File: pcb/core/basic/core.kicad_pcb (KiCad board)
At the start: 2 copper layers, 79.3 x 78.9 mm, 31 parts, among them J1 Conn_01x11, J2 Conn_01x11, J3 Conn_01x04, SW1 SW_Push_45deg, SW10 RotaryEncoder_Switch, SW11 RotaryEncoder_Switch, SW12 RotaryEncoder_Switch, SW13 RotaryEncoder_Switch, SW2 SW_Push_45deg, SW3 SW_Push_45deg, SW4 SW_Push_45deg, SW5 SW_Push_45deg, SW6 SW_Push_45deg, SW7 SW_Push_45deg, SW8 SW_Push_45deg, SW9 SW_Push_45deg, U1 Helios

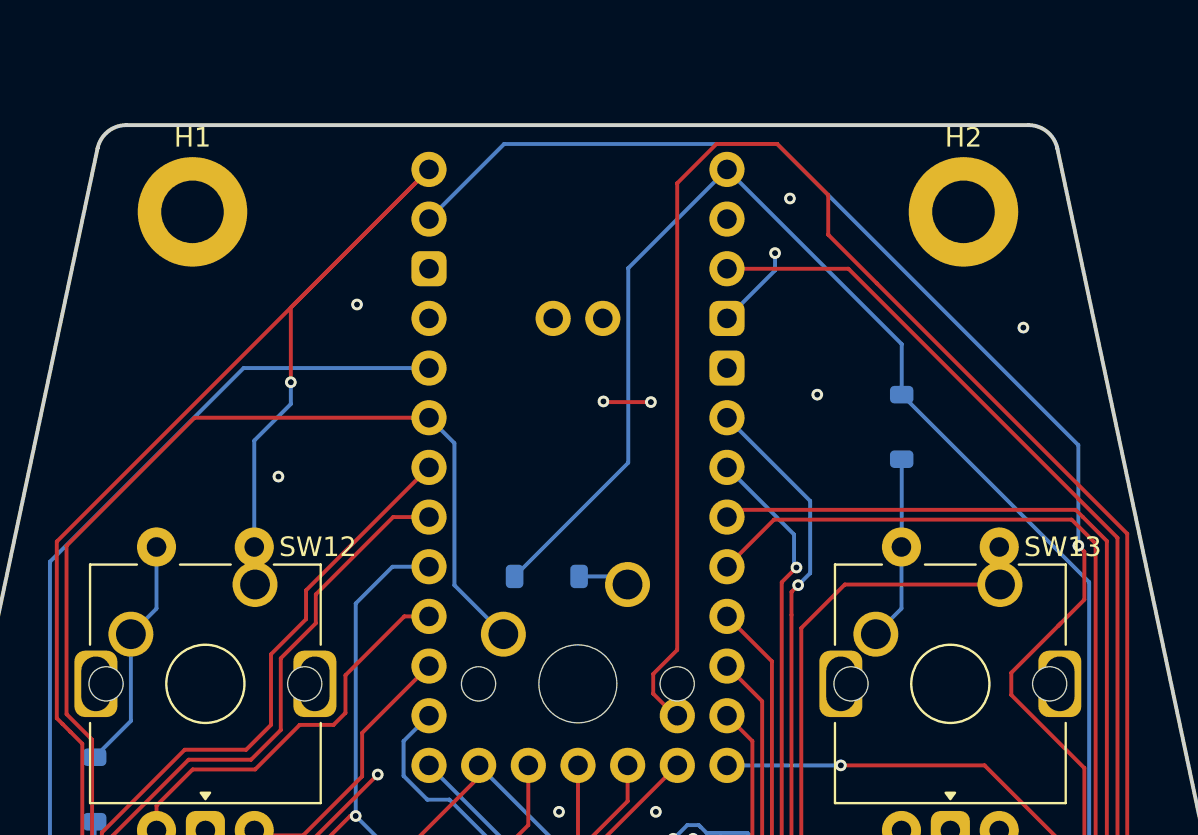
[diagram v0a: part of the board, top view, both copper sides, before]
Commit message: switched rgb back to a regular pin and 3v
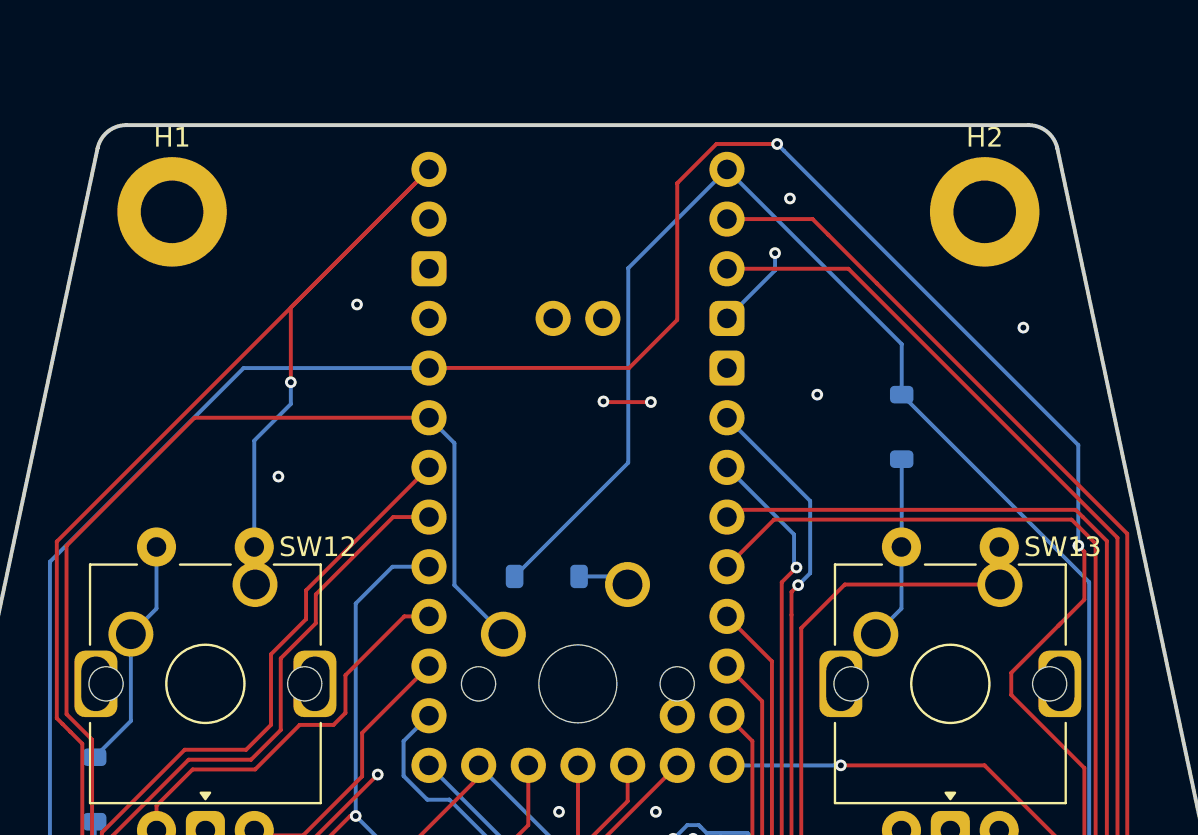
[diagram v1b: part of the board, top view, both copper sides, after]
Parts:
- moved H2 1.09 mm to (219.0, 138.9)
- moved H1 1.04 mm to (177.4, 138.9)
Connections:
- J2 pad 9: raw -> vcc
- U1 pad 1: unconnected-(U1-P0-Pad1) -> rgb
- U1 pad 13: raw -> unconnected-(U1-5V-Pad13)
- U1 pad 34: rgb -> unconnected-(U1-P25-Pad34)
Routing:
- net vcc: track 97.4 -> 203.7 mm, vias 1 -> 3
- net raw: track 99.0 -> 0.00 mm, vias 1 -> 0
- net rgb: track 89.0 -> 54.5 mm

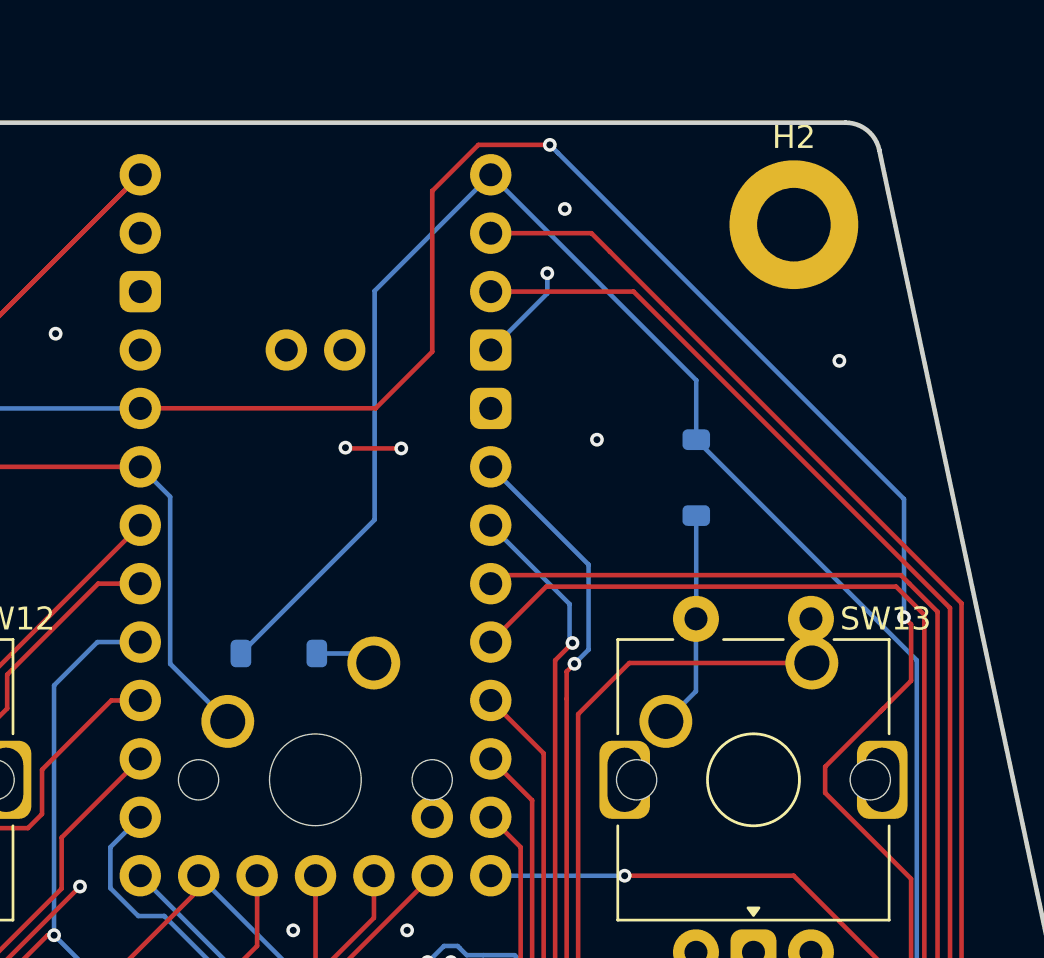
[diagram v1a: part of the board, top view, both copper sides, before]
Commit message: added jumpers for 3.3/5v rgb
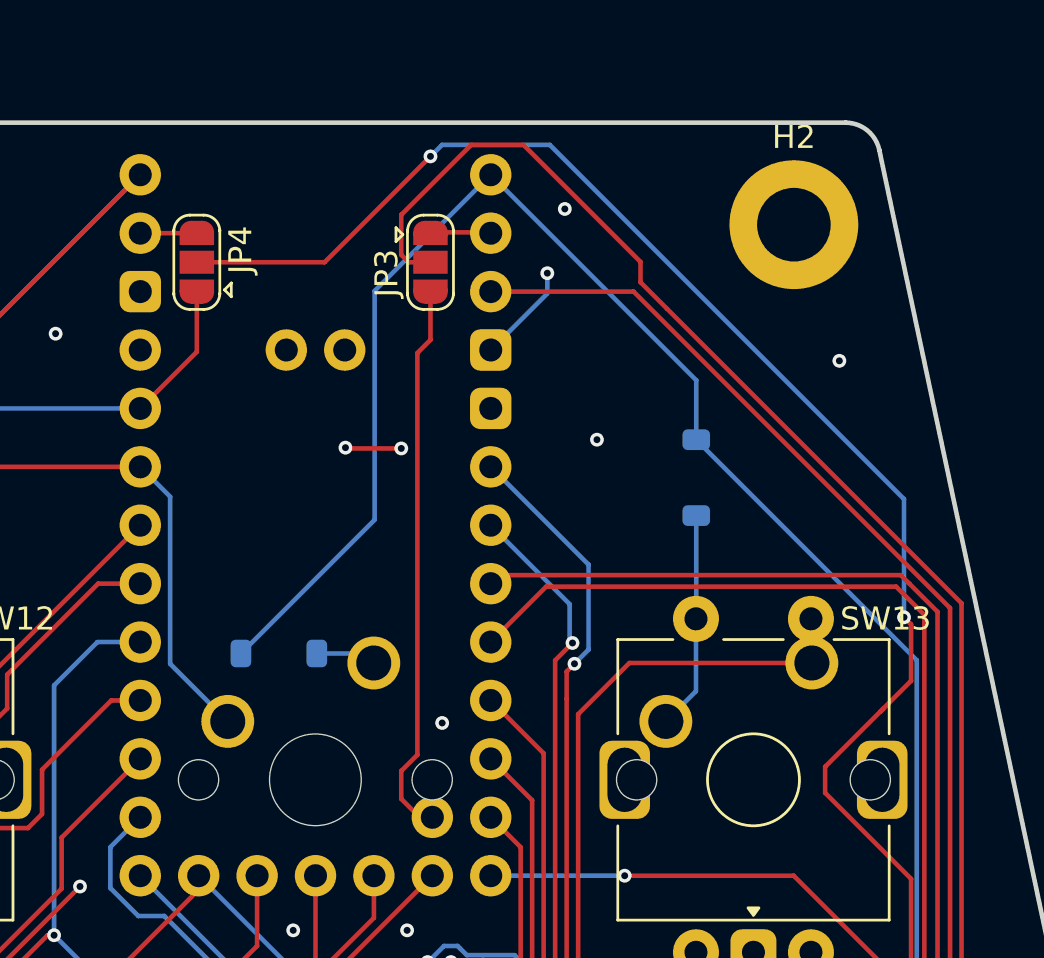
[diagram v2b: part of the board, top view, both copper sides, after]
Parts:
- added JP3: Jumper_3_Open, Jumper:SolderJumper-3_P1.3mm_Open_RoundedPad1.0x1.5mm, F.Cu at (203.2, 140.5)
- added JP4: Jumper_3_Open, Jumper:SolderJumper-3_P1.3mm_Open_RoundedPad1.0x1.5mm, F.Cu at (193.0, 140.5)
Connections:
- J2 pad 9: vcc -> vccrgb
- U1 pad 1: rgb -> Net-(JP3-A)
- U1 pad 13: unconnected-(U1-5V-Pad13) -> Net-(JP4-B)
- U1 pad 34: unconnected-(U1-P25-Pad34) -> Net-(JP3-B)
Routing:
- net vcc: track 203.7 -> 103.5 mm, vias 3 -> 1
- net vccrgb: track 0.00 -> 97.1 mm, vias 0 -> 2
- net Net-(JP3-B): track 0.00 -> 24.3 mm
- net rgb: track 54.5 -> 64.9 mm
- net Net-(JP3-A): track 0.00 -> 2.64 mm
- net Net-(JP4-B): track 0.00 -> 2.53 mm
- net GND: vias 29 -> 30

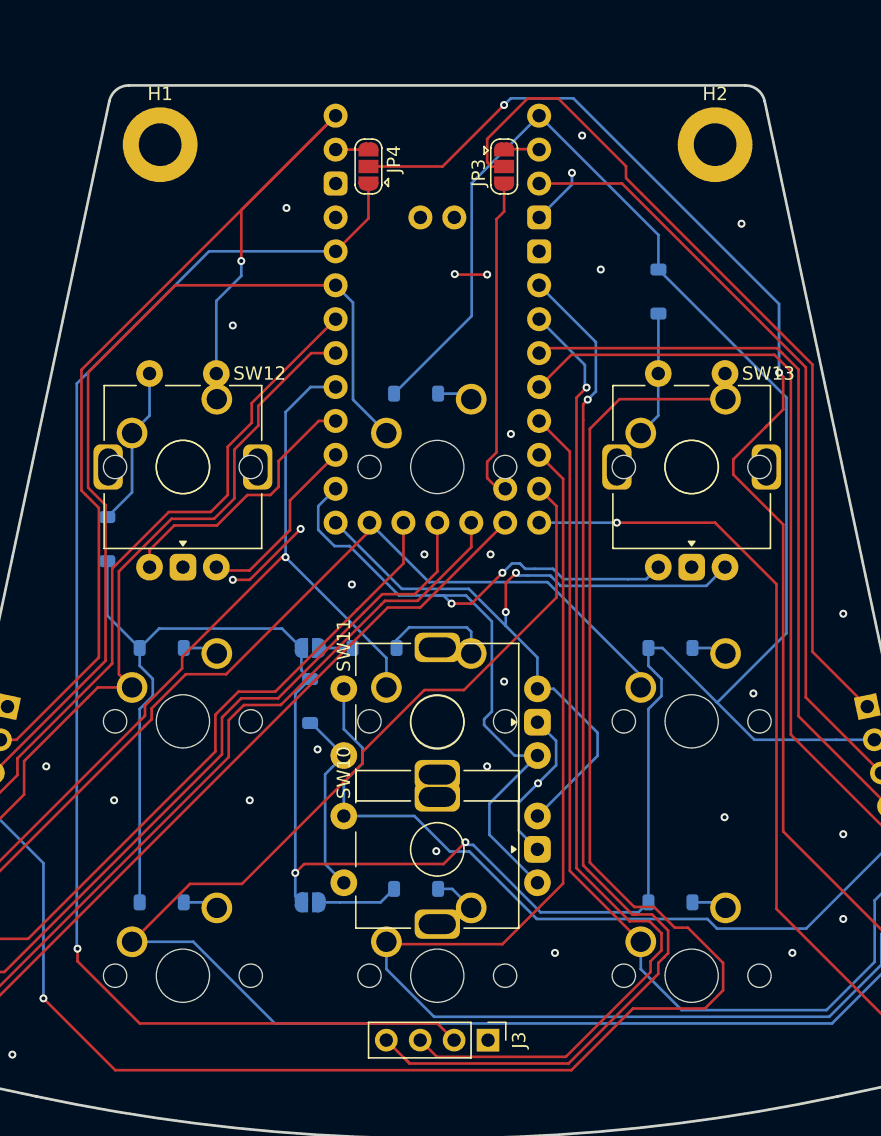
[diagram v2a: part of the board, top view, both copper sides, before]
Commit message: moved rgb jumpers to the other side
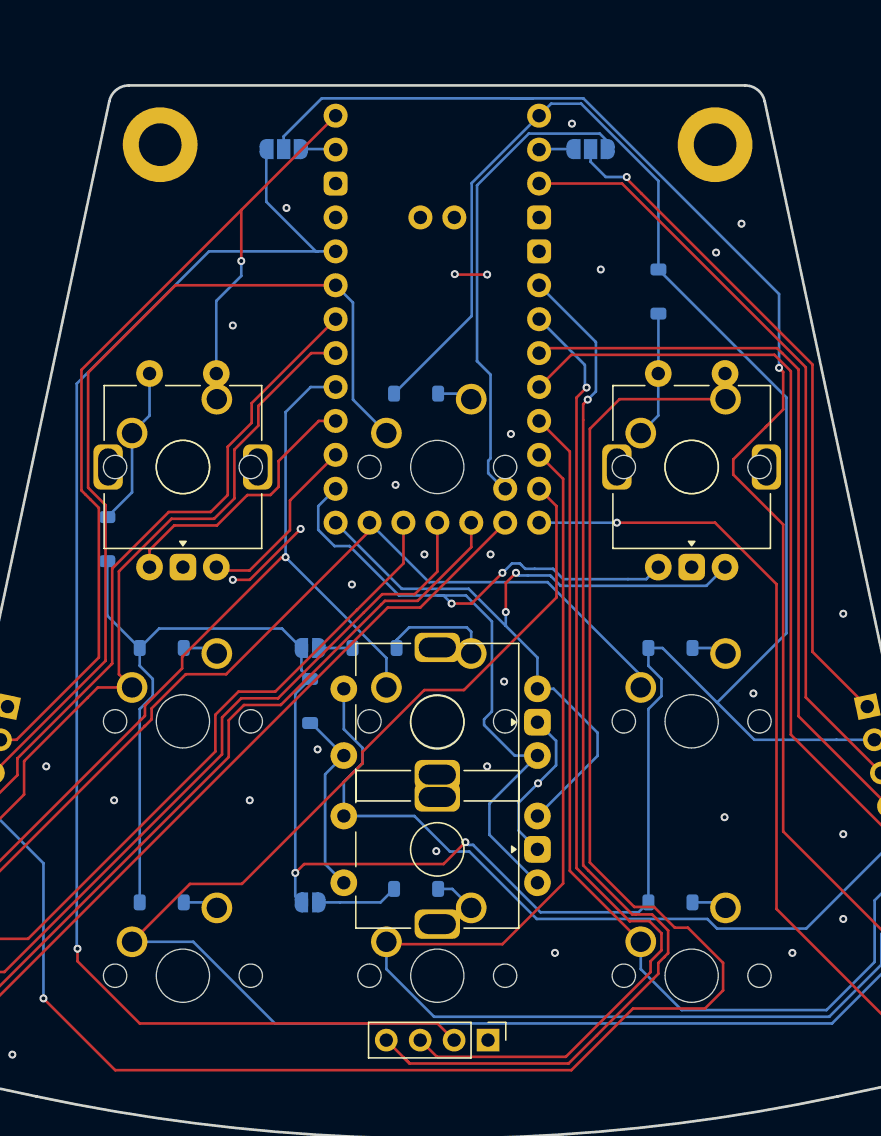
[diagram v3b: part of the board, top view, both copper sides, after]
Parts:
- D1, D10, D2, D3, D4, D5, D6, D7, D8, D9: footprint Diode_SMD:D_SOD-123 -> barnacle:D_SOD-123-minimal
- JP3, JP4: moved to B.Cu
- moved JP3 6.61 mm to (209.7, 139.2), turned to 180 degrees
- moved JP4 6.48 mm to (186.7, 139.2), turned to 180 degrees
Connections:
- JP4 pad 1: vcc -> Net-(JP4-A)
- JP4 pad 3: Net-(JP4-B) -> vcc
- U1 pad 1: Net-(JP3-A) -> Net-(JP3-B)
- U1 pad 13: Net-(JP4-B) -> Net-(JP4-A)
- U1 pad 34: Net-(JP3-B) -> Net-(JP3-A)
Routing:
- net Net-(JP3-A): track 2.64 -> 36.7 mm
- net Net-(JP3-B): track 24.3 -> 2.62 mm
- net rgb: track 64.9 -> 51.2 mm, vias 0 -> 1
- net col0: track 82.5 -> 72.5 mm
- net vccrgb: track 97.1 -> 105.5 mm, vias 2 -> 1
- net GND: track 25.4 -> 21.0 mm, vias 30 -> 31
- net vcc: track 103.5 -> 106.7 mm
- net row5: track 209.3 -> 212.4 mm
- net Net-(JP4-A): track 0.00 -> 2.66 mm
- net Net-(JP4-B): track 2.53 -> 0.00 mm
